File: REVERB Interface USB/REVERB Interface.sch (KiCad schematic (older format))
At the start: 74 parts, among them J1 RPiZeroW, J2 Iridium, J3 APRS, J4 Antenna, J6 USB_B_Micro, J7 USB, J8 USBPOGO, M1 MountingHole_Pad, M2 MountingHole_Pad, M3 MountingHole_Pad, M4 MountingHole_Pad, M5 PiMount, M6 PiMount, M7 PiMount, M8 PiMount, U1 IMU, U2 MAX3232, U3 CY7C65213-28PVXI, U4 TXB0104D

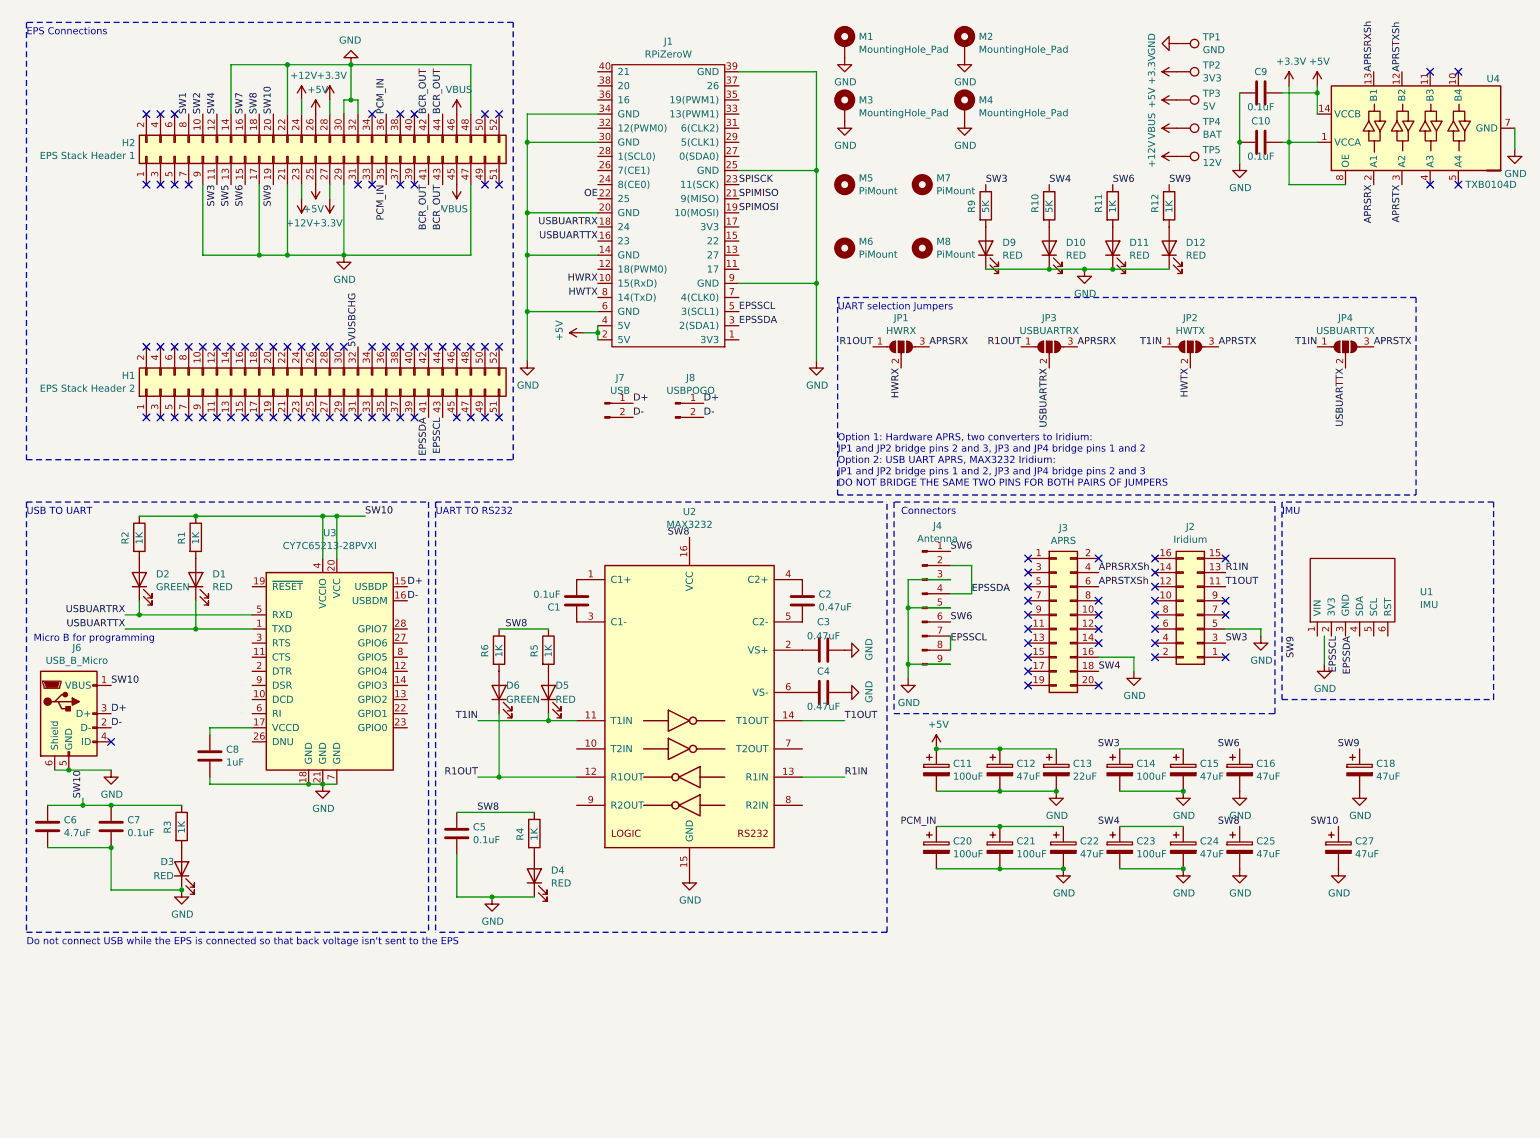
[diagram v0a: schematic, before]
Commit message: finish bno055 mod, push v1.5
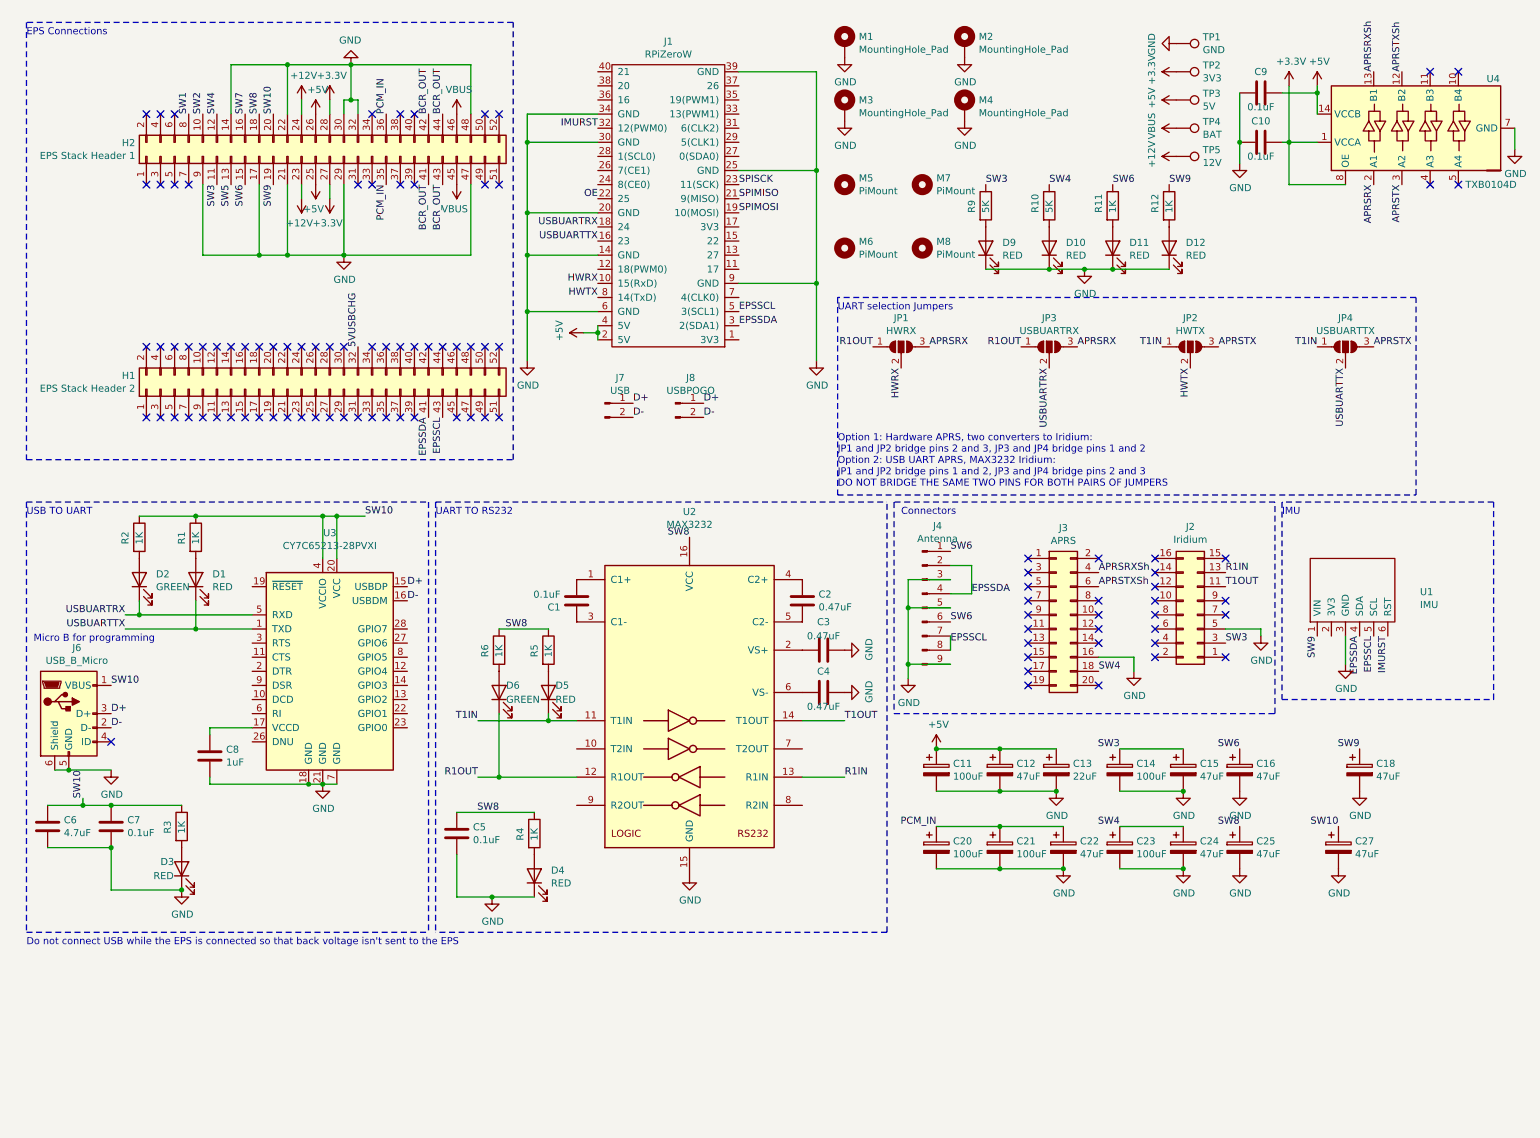
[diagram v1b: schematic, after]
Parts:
- U1: footprint REVERB Interface:LSM9DS1-BNO055 -> REVERB Interface:BNO055
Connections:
- net EPSSCL: now also U1.5 (SCL)
- net EPSSDA: now also U1.4 (SDA)
- net GND: now also U1.3 (GND)
- net SW9: now also U1.1 (VIN)
- net IMURST: now reaches J1.32 (12(PWM0))
- net IMURST: now also U1.6 (RST)
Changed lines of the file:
@@
 Title "TJ REVERB Interface Board"
 Date "2021-10-03"
-Rev "1.3"
+Rev "1.5"
 Comp "TJ Nanosat Club"
 Comment1 "Redesign from previous Eagle designs"
@@
 Wire Notes Line
 	6600 6950 6600 3900
-Text Label 9500 4850 3    50   ~ 0
+Text Label 9650 4850 3    50   ~ 0
 SW9
 Wire Wire Line
-	9700 4850 9700 5050
+	9850 4850 9850 5050
 $Comp
 L power:GND #PWR0129
 U 1 1 617E7DA1
-P 9700 5050
-F 0 "#PWR0129" H 9700 4800 50  0001 C CNN
-F 1 "GND" H 9705 4877 50  0000 C CNN
-F 2 "" H 9700 5050 50  0001 C CNN
-F 3 "" H 9700 5050 50  0001 C CNN
-	1    9700 5050
-	1    0    0    -1
-$EndComp
-Text Label 9800 4850 3    50   ~ 0
+P 9850 5050
+F 0 "#PWR0129" H 9850 4800 50  0001 C CNN
+F 1 "GND" H 9855 4877 50  0000 C CNN
+F 2 "" H 9850 5050 50  0001 C CNN
+F 3 "" H 9850 5050 50  0001 C CNN
+	1    9850 5050
+	1    0    0    -1
+$EndComp
+Text Label 10050 4850 3    50   ~ 0
 EPSSCL
-Text Label 9900 4850 3    50   ~ 0
+Text Label 9950 4850 3    50   ~ 0
 EPSSDA
 Text Notes 9400 4000 0    50   ~ 0
@@
 F 0 "U1" H 10378 4363 50  0000 L CNN
 F 1 "IMU" H 10378 4272 50  0000 L CNN
-F 2 "REVERB Interface:LSM9DS1-BNO055" H 9900 4450 50  0001 C CNN
+F 2 "REVERB Interface:BNO055" H 9900 4450 50  0001 C CNN
 F 3 "" H 9900 4450 50  0001 C CNN
 	1    9900 4450
 	1    0    0    -1
 $EndComp
+Text Label 10150 4850 3    50   ~ 0
+IMURST
+Text Label 4550 1250 2    50   ~ 0
+IMURST
 $EndSCHEMATC

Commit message: RI line
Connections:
- net GND: now also J2.15 (Pin_15)
- net RI: now reaches J1.12 (18(PWM0))
- net RI: now also J2.8 (Pin_8)
- no-connect marks 100 -> 98
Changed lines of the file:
@@
 NoConn ~ 8500 4500
 NoConn ~ 8500 4600
-NoConn ~ 8500 4700
 NoConn ~ 8500 4800
 NoConn ~ 8500 4900
 NoConn ~ 8500 5000
-NoConn ~ 9000 4300
 NoConn ~ 9000 4600
 NoConn ~ 9000 4700
@@
 Text Label 4550 1250 2    50   ~ 0
 IMURST
+Text Label 8500 4700 2    50   ~ 0
+RI
+Text Label 4550 2250 2    50   ~ 0
+RI
+Wire Wire Line
+	9250 4800 9250 4300
+Wire Wire Line
+	9250 4300 9000 4300
+Connection ~ 9250 4800
 $EndSCHEMATC

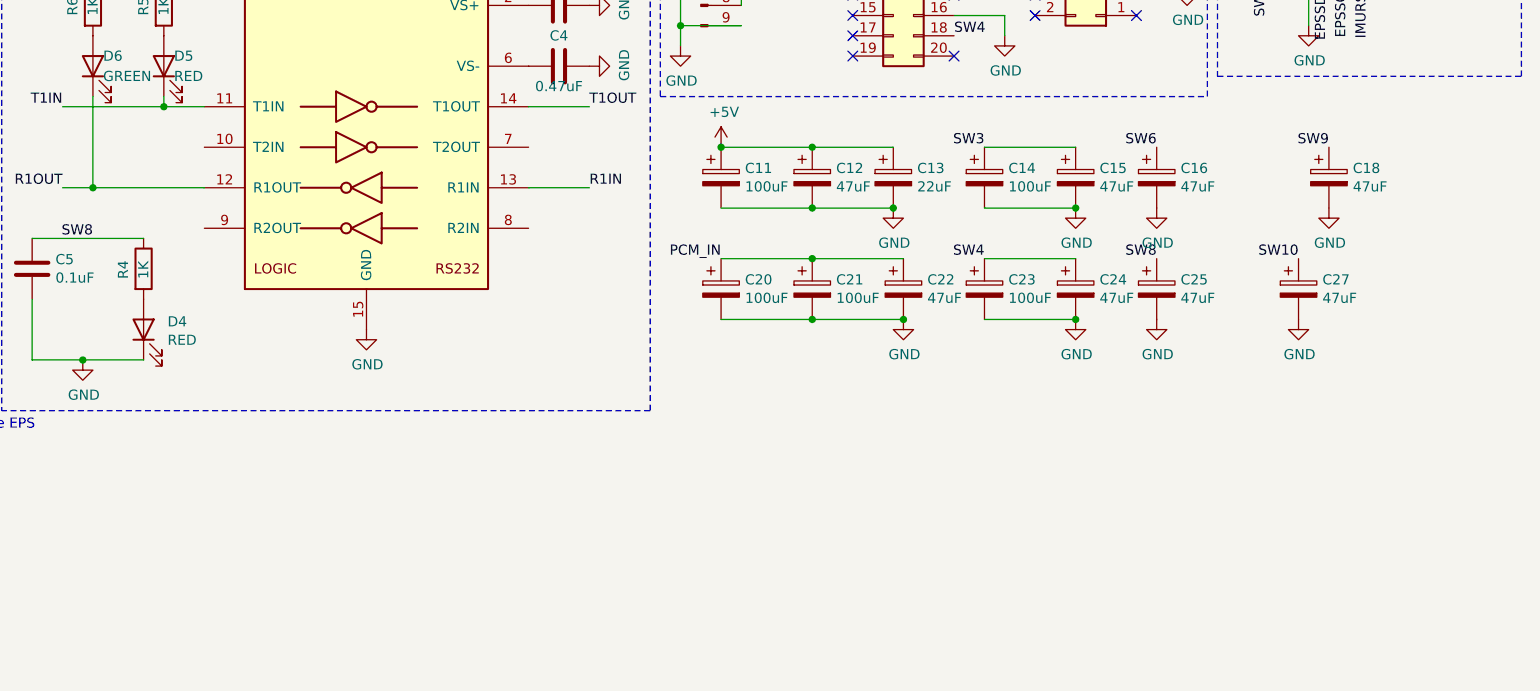
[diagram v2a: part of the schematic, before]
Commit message: implement rtc on a pdm
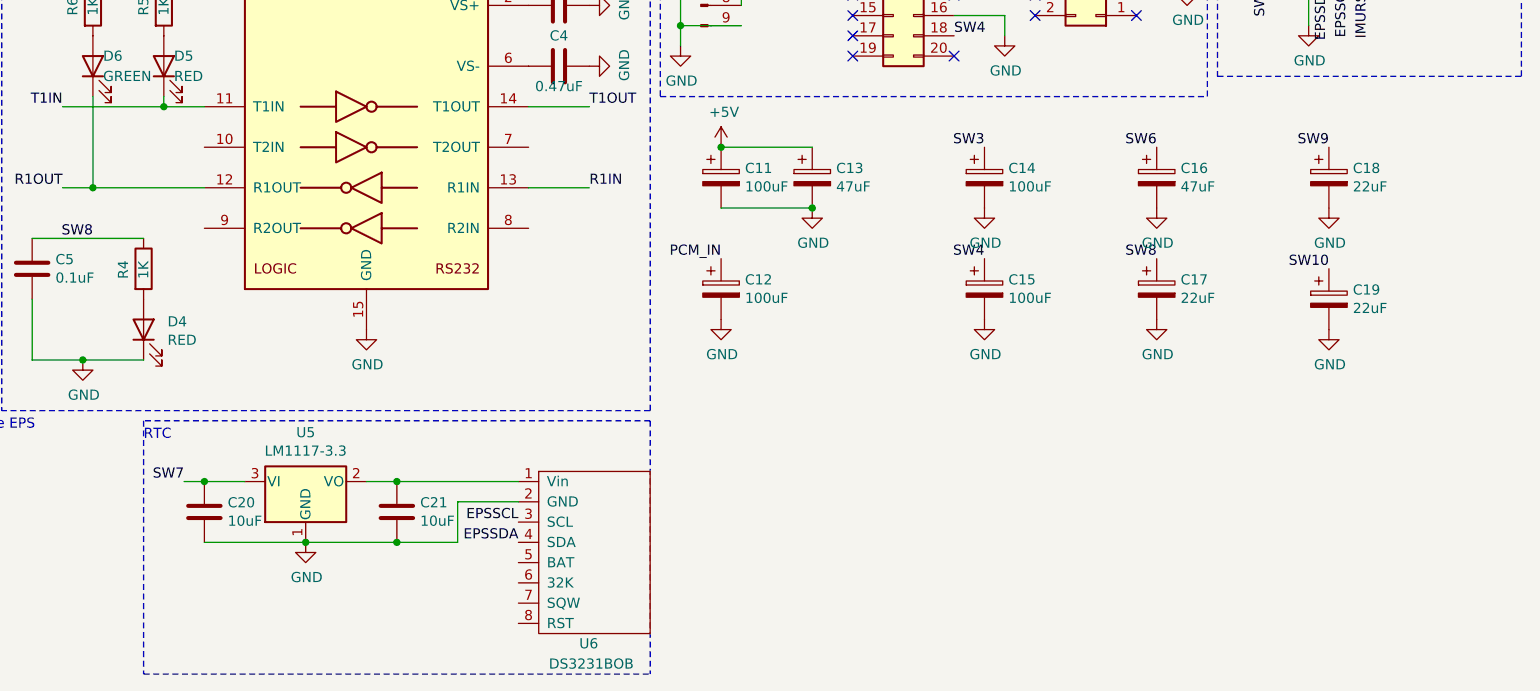
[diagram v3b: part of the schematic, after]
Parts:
- removed C20, C21, C23: 100uF, Capacitor_Tantalum_SMD:CP_EIA-7343-43_Kemet-X_Pad2.25x2.55mm_HandSolder, symbol Device:CP
- removed C22, C24, C25, C27: 47uF, Capacitor_Tantalum_SMD:CP_EIA-6032-28_Kemet-C_Pad2.25x2.35mm_HandSolder, symbol Device:CP
- added C17, C19: 22uF, Capacitor_Tantalum_SMD:CP_EIA-6032-28_Kemet-C_Pad2.25x2.35mm_HandSolder, symbol Device:CP
- added C20, C21: 10uF, Capacitor_SMD:C_0805_2012Metric_Pad1.18x1.45mm_HandSolder, symbol Device:C
- added U5: LM1117-3.3, Package_TO_SOT_SMD:SOT-223-3_TabPin2, symbol Regulator_Linear:LM1117-3.3
- added U6: DS3231BOB, REVERB Interface:DS3231BOB, symbol REVERBSym:DS3231BOB
- C12, C15: value 47uF -> 100uF; footprint Capacitor_Tantalum_SMD:CP_EIA-6032-28_Kemet-C_Pad2.25x2.35mm_HandSolder -> Capacitor_Tantalum_SMD:CP_EIA-7343-43_Kemet-X_Pad2.25x2.55mm_HandSolder
- C13: value 22uF -> 47uF
- C18: value 47uF -> 22uF
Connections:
- net +5V: no longer C12.1
- net EPSSCL: now also U6.3 (SCL)
- net EPSSDA: now also U6.4 (SDA)
- net GND: now also C17.2, C19.2, C20.2, C21.2, U5.1 (GND), U6.2 (GND)
- net PCM_IN: now also C12.1
- net SW10: now also C19.1
- net SW3: no longer C15.1
- net SW4: now also C15.1
- net SW7: now also C20.1, U5.3 (VI)
- net SW8: now also C17.1
- new net: C21.1, U5.2 (VO), U6.1 (Vin)
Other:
- note added: "RTC"

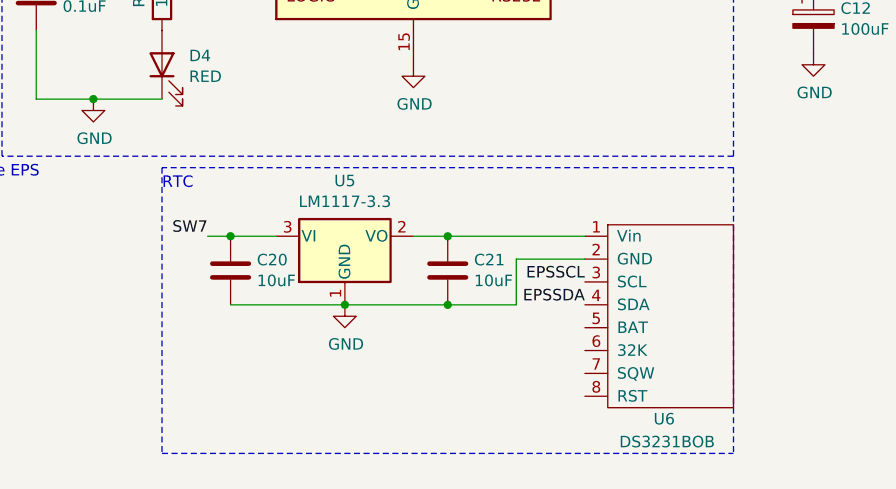
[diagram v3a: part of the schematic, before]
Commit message: embed the rtc
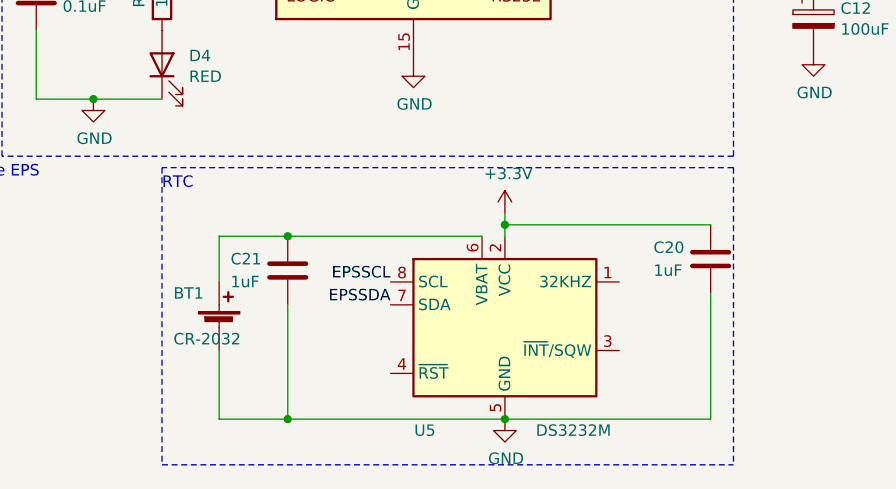
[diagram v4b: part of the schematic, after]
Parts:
- removed U5: LM1117-3.3, Package_TO_SOT_SMD:SOT-223-3_TabPin2, symbol Regulator_Linear:LM1117-3.3
- removed U6: DS3231BOB, REVERB Interface:DS3231BOB, symbol REVERBSym:DS3231BOB
- added BT1: CR-2032, symbol Device:Battery_Cell
- added U5: DS3232M, Package_SO:SOIC-8_3.9x4.9mm_P1.27mm, symbol Timer_RTC:DS3232M
- C20, C21: value 10uF -> 1uF
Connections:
- net +3V3: now also C20.1, U5.2 (VCC)
- net EPSSCL: now also U5.8 (SCL)
- net EPSSDA: now also U5.7 (SDA)
- net GND: now also BT1.2 (-), U5.5 (GND)
- net SW7: no longer C20.1
- net at C21.1: now also BT1.1 (+), U5.6 (VBAT)
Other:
- moved on the sheet: C20
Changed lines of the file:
@@
 	1    0    0    -1
 $EndComp
-$Comp
-L REVERBSym:DS3231BOB U6
-U 1 1 61A71857
-P 6300 7650
-F 0 "U6" V 6750 7600 50  0000 L CNN
-F 1 "DS3231BOB" V 6850 7450 50  0000 L CNN
-F 2 "REVERB Interface:DS3231BOB" H 6300 7650 50  0001 C CNN
-F 3 "" H 6300 7650 50  0001 C CNN
-	1    6300 7650
-	0    1    1    0
-$EndComp
-$Comp
-L Regulator_Linear:LM1117-3.3 U5
-U 1 1 61A7185D
-P 4900 7300
-F 0 "U5" H 4900 7542 50  0000 C CNN
-F 1 "LM1117-3.3" H 4900 7451 50  0000 C CNN
-F 2 "Package_TO_SOT_SMD:SOT-223-3_TabPin2" H 4900 7300 50  0001 C CNN
-F 3 "http://www.ti.com/lit/ds/symlink/lm1117.pdf" H 4900 7300 50  0001 C CNN
-	1    4900 7300
-	1    0    0    -1
-$EndComp
-Text Label 5950 7500 2    50   ~ 0
+Text Label 5100 7500 2    50   ~ 0
 EPSSCL
-Text Label 5950 7600 2    50   ~ 0
+Text Label 5100 7600 2    50   ~ 0
 EPSSDA
-Text Label 4300 7300 2    50   ~ 0
-SW7
-$Comp
-L Device:C C20
-U 1 1 61A71866
-P 4400 7450
-F 0 "C20" H 4515 7496 50  0000 L CNN
-F 1 "10uF" H 4515 7405 50  0000 L CNN
-F 2 "Capacitor_SMD:C_0805_2012Metric_Pad1.18x1.45mm_HandSolder" H 4438 7300 50  0001 C CNN
-F 3 "~" H 4400 7450 50  0001 C CNN
-	1    4400 7450
-	1    0    0    -1
-$EndComp
-$Comp
-L Device:C C21
-U 1 1 61A7186C
-P 5350 7450
-F 0 "C21" H 5465 7496 50  0000 L CNN
-F 1 "10uF" H 5465 7405 50  0000 L CNN
-F 2 "Capacitor_SMD:C_0805_2012Metric_Pad1.18x1.45mm_HandSolder" H 5388 7300 50  0001 C CNN
-F 3 "~" H 5350 7450 50  0001 C CNN
-	1    5350 7450
-	1    0    0    -1
-$EndComp
-Wire Wire Line
-	4300 7300 4400 7300
-Connection ~ 4400 7300
-Wire Wire Line
-	4400 7300 4600 7300
-Wire Wire Line
-	5200 7300 5350 7300
-Connection ~ 5350 7300
-Wire Wire Line
-	5350 7300 5950 7300
-Wire Wire Line
-	4400 7600 4900 7600
-Wire Wire Line
-	5650 7600 5650 7400
-Wire Wire Line
-	5650 7400 5950 7400
-Connection ~ 4900 7600
-Wire Wire Line
-	4900 7600 5350 7600
-Connection ~ 5350 7600
-Wire Wire Line
-	5350 7600 5650 7600
 $Comp
 L power:GND #PWR014
 U 1 1 61A7187F
-P 4900 7600
-F 0 "#PWR014" H 4900 7350 50  0001 C CNN
-F 1 "GND" H 4905 7427 50  0000 C CNN
-F 2 "" H 4900 7600 50  0001 C CNN
-F 3 "" H 4900 7600 50  0001 C CNN
-	1    4900 7600
+P 5600 8100
+F 0 "#PWR014" H 5600 7850 50  0001 C CNN
+F 1 "GND" H 5605 7927 50  0000 C CNN
+F 2 "" H 5600 8100 50  0001 C CNN
+F 3 "" H 5600 8100 50  0001 C CNN
+	1    5600 8100
 	1    0    0    -1
 $EndComp
@@
 RTC
 Wire Notes Line
-	4100 7000 4100 8250
-Wire Notes Line
-	4100 8250 6600 8250
+	4100 8300 6600 8300
 Wire Notes Line
 	6600 7000 4100 7000
+$Comp
+L Device:Battery_Cell BT1
+U 1 1 61948908
+P 4350 7700
+F 0 "BT1" H 4150 7850 50  0000 L CNN
+F 1 "CR-2032" H 4150 7650 50  0000 L CNN
+F 2 "" V 4350 7760 50  0001 C CNN
+F 3 "~" V 4350 7760 50  0001 C CNN
+	1    4350 7700
+	1    0    0    -1
+$EndComp
+$Comp
+L power:+3.3V #PWR?
+U 1 1 6194BC39
+P 5600 7200
+F 0 "#PWR?" H 5600 7050 50  0001 C CNN
+F 1 "+3.3V" H 5615 7373 50  0000 C CNN
+F 2 "" H 5600 7200 50  0001 C CNN
+F 3 "" H 5600 7200 50  0001 C CNN
+	1    5600 7200
+	1    0    0    -1
+$EndComp
+Wire Wire Line
+	5600 7200 5600 7250
+Wire Wire Line
+	5600 7250 6500 7250
+Connection ~ 5600 7250
+Wire Wire Line
+	5600 7250 5600 7300
+Wire Wire Line
+	5600 8100 6500 8100
+Wire Wire Line
+	6500 8100 6500 7550
+$Comp
+L Device:C C20
+U 1 1 61A71866
+P 6500 7400
+F 0 "C20" H 6250 7450 50  0000 L CNN
+F 1 "1uF" H 6250 7350 50  0000 L CNN
+F 2 "Capacitor_SMD:C_0805_2012Metric_Pad1.18x1.45mm_HandSolder" H 6538 7250 50  0001 C CNN
+F 3 "~" H 6500 7400 50  0001 C CNN
+	1    6500 7400
+	1    0    0    -1
+$EndComp
+Wire Wire Line
+	4350 7800 4350 8100
+Connection ~ 5600 8100
+Wire Wire Line
+	5500 7300 4650 7300
+Wire Wire Line
+	4350 7300 4350 7500
 Wire Notes Line
-	6600 7000 6600 8250
+	6600 7000 6600 8300
+Wire Notes Line
+	4100 7000 4100 8300
+$Comp
+L Device:C C21
+U 1 1 619A650B
+P 4650 7450
+F 0 "C21" H 4400 7500 50  0000 L CNN
+F 1 "1uF" H 4400 7400 50  0000 L CNN
+F 2 "Capacitor_SMD:C_0805_2012Metric_Pad1.18x1.45mm_HandSolder" H 4688 7300 50  0001 C CNN
+F 3 "~" H 4650 7450 50  0001 C CNN
+	1    4650 7450
+	1    0    0    -1
+$EndComp
+Connection ~ 4650 7300
+Wire Wire Line
+	4350 8100 4650 8100
+Wire Wire Line
+	4350 7300 4650 7300
+Wire Wire Line
+	4650 7600 4650 8100
+Connection ~ 4650 8100
+Wire Wire Line
+	4650 8100 5600 8100
+$Comp
+L Timer_RTC:DS3232M U5
+U 1 1 61946807
+P 5600 7700
+F 0 "U5" H 5250 7250 50  0000 C CNN
+F 1 "DS3232M" H 5900 7250 50  0000 C CNN
+F 2 "Package_SO:SOIC-8_3.9x4.9mm_P1.27mm" H 5650 7200 50  0001 C CNN
+F 3 "http://datasheets.maximintegrated.com/en/ds/DS3232M.pdf" H 5870 7850 50  0001 C CNN
+	1    5600 7700
+	1    0    0    -1
+$EndComp
 $EndSCHEMATC
